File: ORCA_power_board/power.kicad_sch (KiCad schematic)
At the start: 70 parts, among them J4 emergence, Q1 TJ60S04M3L, Q2 BSS138, Q3 BSS138, Q4 IRLML6402, U1 LTC2301IMS, U2 NJM78055DL1, U4 RH1B-UDC6V, U5 TPH11006NL, U6 TPH11006NL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

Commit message: fixed most of the error. waiting check
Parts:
- removed Q4: IRLML6402, Package_TO_SOT_SMD:SOT-23, symbol Transistor_FET:IRLML6402
- added Q4: BSS138, Package_TO_SOT_SMD:SOT-23, symbol Transistor_FET:BSS138
- R13: value 4.7k -> 4.7
- U1: footprint Package_DFN_QFN:TDFN-12_2x3mm_P0.5mm -> Package_SO:MSOP-12_3x4mm_P0.65mm
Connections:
- net +3V3_power: now also Q2.1 (G), Q3.1 (G), R7.1, R9.1
- net +5V_power: now also U2.3 (Vout); no longer U2.2 (Vout)
- net +6V_power: now also U2.1 (Vin); no longer R11.2, U2.3 (Vin)
- net +BATT_power: now also Q1.3 (S); no longer Q1.1 (D)
- net +VDD_power: now also R13.1; no longer R13.2
- net GND: now also U2.2 (GND), U5.1, U5.2, U5.3, U6.1, U6.2, U6.3; no longer U2.1 (GND), U5.5, U5.6, U5.7, U5.8, U6.5, U6.6, U6.7, U6.8
- net VBUS_power: no longer Q2.1 (G), Q3.1 (G), R7.1, R9.1
- net Vout_motor: now also R11.2, Q4.1 (G)
- net power_checker: now also Q4.2 (S)
- net at Q1.2 (G): now also R13.2; no longer R13.1
- net at D14.1 (K), F1.1: now also Q1.1 (D); no longer Q1.3 (S)
- net at D6.1 (K), J4.1 (Pin_1), R18.1: now also U5.5, U5.6, U5.7, U5.8; no longer U5.1, U5.2, U5.3
- net at R11.1, R17.2: now also Q4.3 (D)
- new net: D8.1 (K), R19.2, U6.5, U6.6, U6.7, U6.8
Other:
- moved on the sheet: C21, C22, C23, C4, D1, D14, D2, Q1, R1, R13, R2

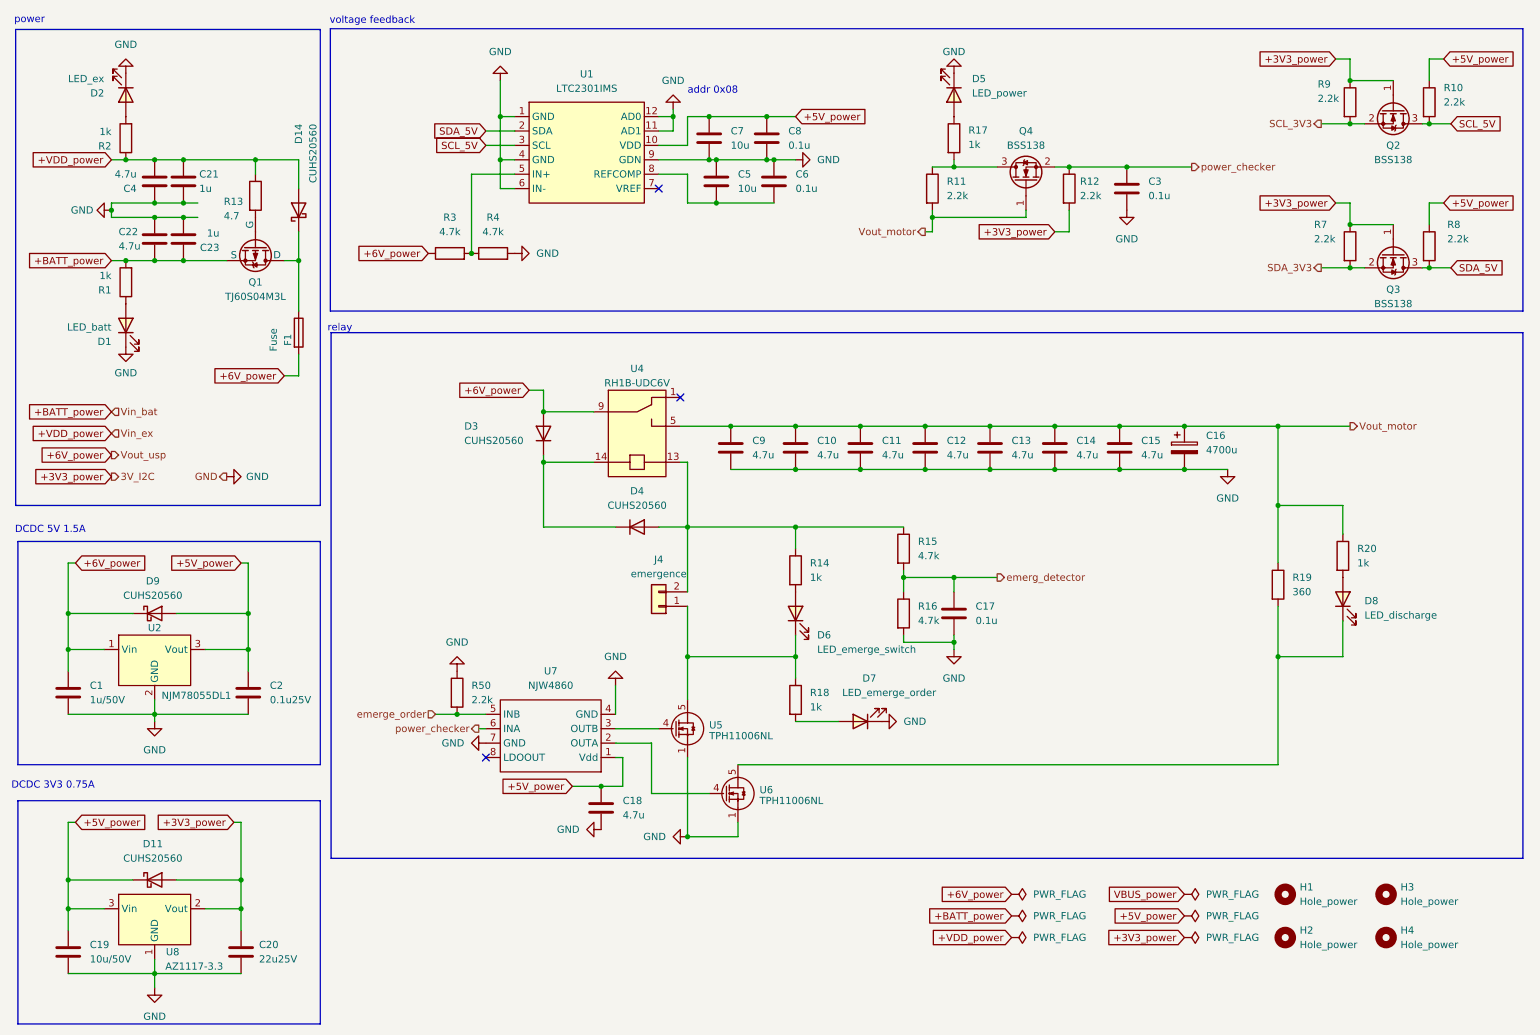
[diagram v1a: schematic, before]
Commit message: add power registers to power_board gate driver
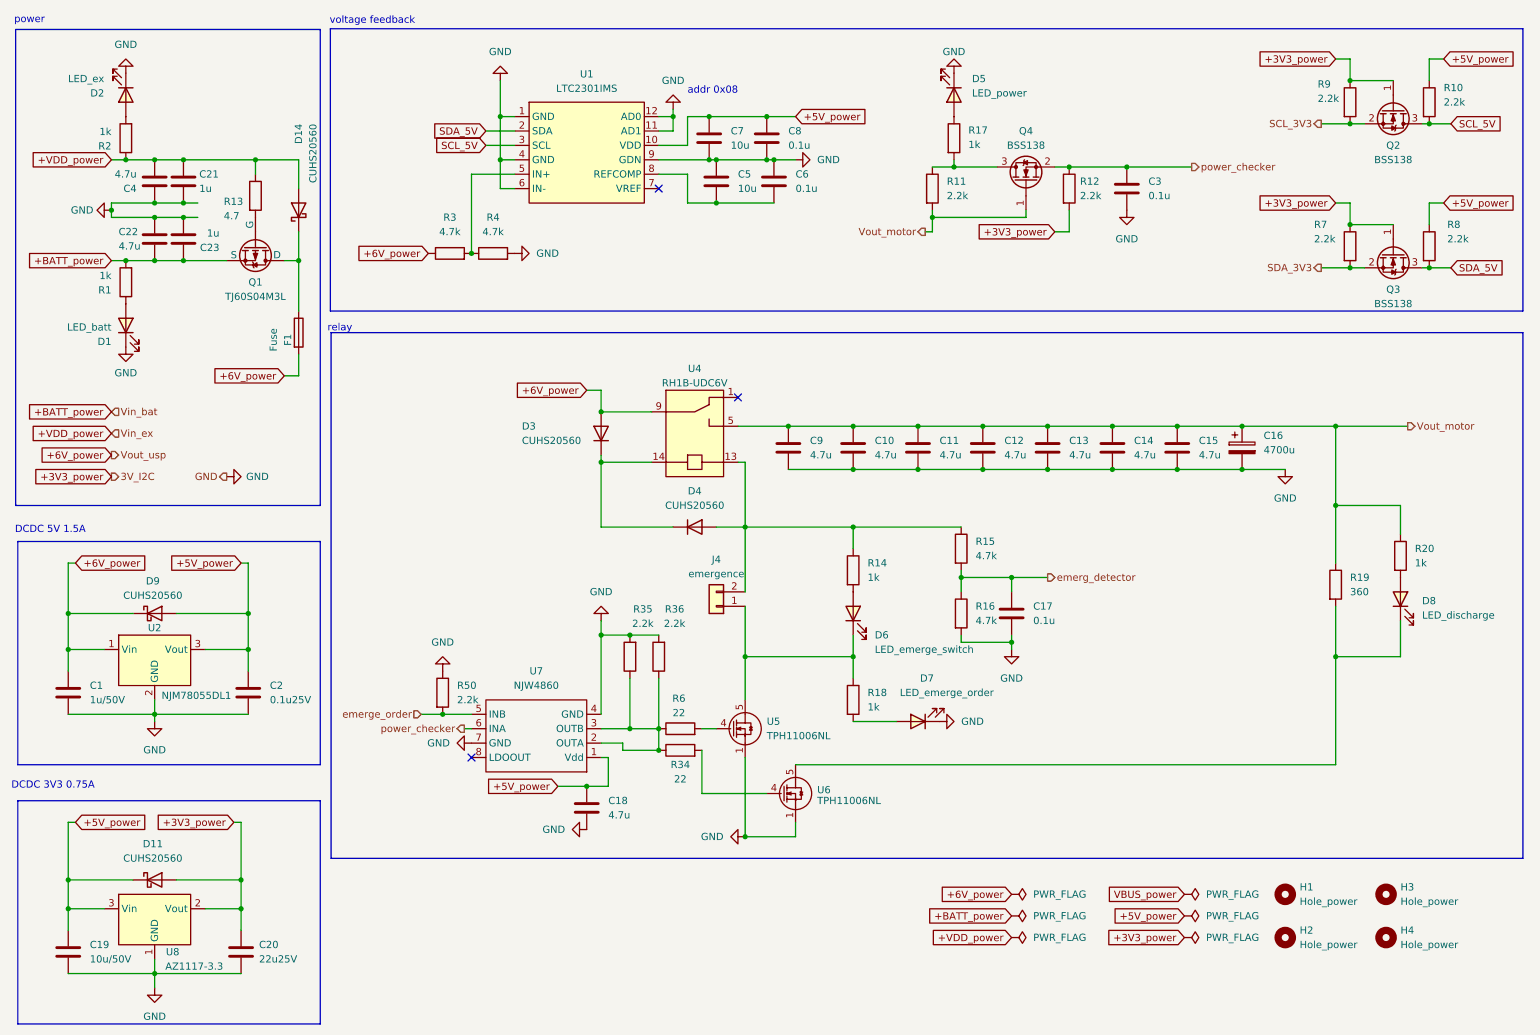
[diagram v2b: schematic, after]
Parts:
- added R34, R6: 22, Resistor_SMD:R_0603_1608Metric_Pad0.98x0.95mm_HandSolder, symbol Device:R
- added R35, R36: 2.2k, Resistor_SMD:R_0603_1608Metric_Pad0.98x0.95mm_HandSolder, symbol Device:R
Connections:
- net GND: now also R35.2, R36.2
- net at U6.4: now also R34.2; no longer U7.2 (OUTA)
- net at U7.3 (OUTB): now also U7.2 (OUTA), R34.1, R35.1, R36.1, R6.1; no longer U5.4
- new net: R6.2, U5.4
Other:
- moved on the sheet: C10, C11, C12, C13, C14, C15, C16, C17, C18, C9, D3, D4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
